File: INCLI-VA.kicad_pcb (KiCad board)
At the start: 2 copper layers, 100 x 100 mm, 168 parts, among them J1 MSTBV 2,5/5-GF-5,08, J2 MSTBV 2,5/2-GF-5,08, J401 USB4105-GF-A, J402 UART0, Q101 STD18NF25, Q102 IPD30N10S3L-34, Q701 DMN10H220LQ, Q751 DMN10H220LQ, SW401 RESET, SW402 BOOT, U101 LM74930QRGERQ1, U201 LMR38010SQDDARQ1, U301 TPS62A02QDRLRQ1, U302 LP5907QMFX-3.3Q1, U401 ESP32-S3-WROOM-1-N8R2, U402 USBLC6-2SC6, U501 SCL3300-D01, U502 ASM330LHHTR, U503 AS5147U-HTSM, U601 ADM3055E, U701 74AHCT1G126, U751 74AHCT1G126, U801 TPS3828-33Q1

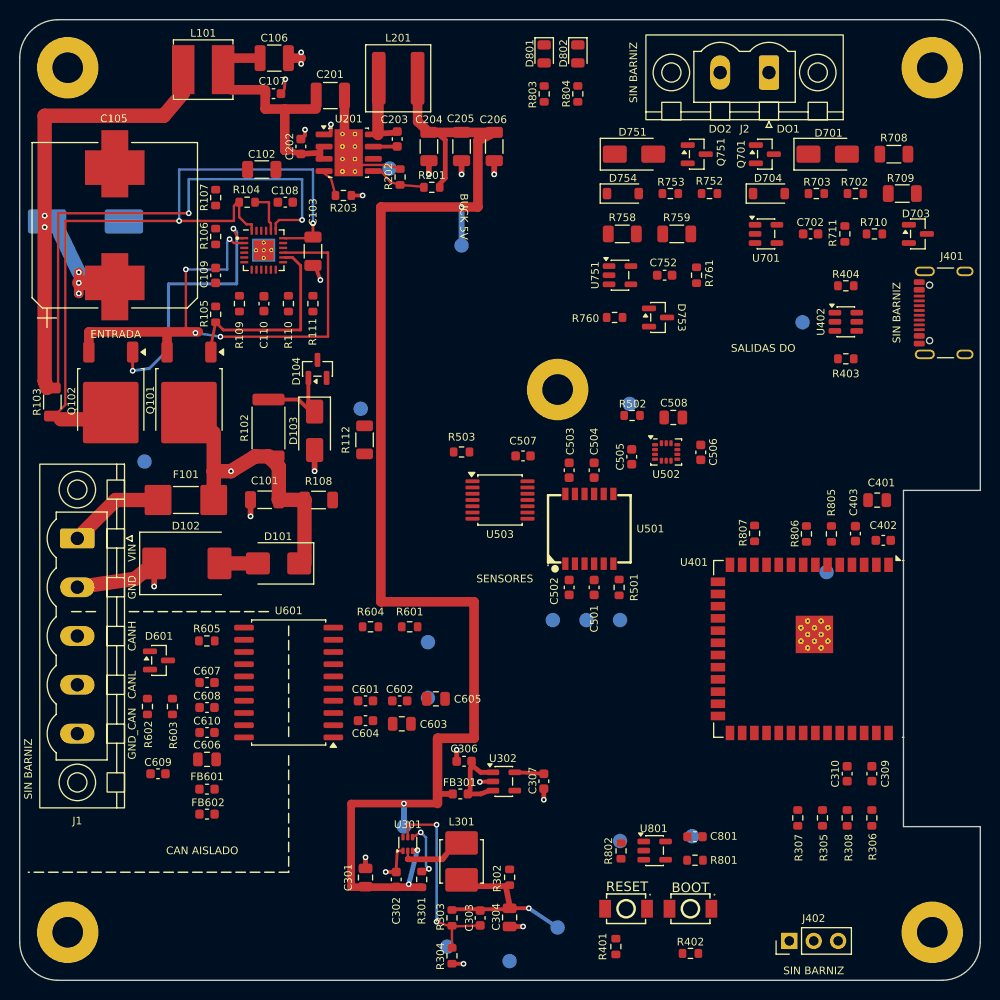
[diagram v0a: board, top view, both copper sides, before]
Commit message: [Claude Code] ruteo etapa 1 (cierre): net class PROT, lazo de U201 en F.Cu, U301 girado, gates paralelos y traspaso a Codex
- Net class PROT (VA, C_ID, VOUT, +VPROT) a 0.6 mm; HV solo VIN_VEH/VBAT_F (1.25 mm).
- ZONA_BUCK_U201 a 0.25 mm: retorno de C202 directo al pin 1 y EP (lazo 6.1 -> 3.9 mm2);
  C201 -> VIN 11.3 -> 8.6 mm.
- U301 girado 180 grados y C302 junto a VIN: SW al norte en F.Cu, EN/FB/PG al sur sin cruzarlo.
- TP101 a (127.6, 61.5) conectado a +VPROT.
- HGATE paralela a OUT/VA; DGATE por B.Cu bajo el retorno de A/VA.
- C104 sigue en B.Cu; caja con separadores >= 12 mm y adhesivo en C104.
- docs/RUTEO_TRASPASO.md: estado, reglas, restricciones, plan de etapas 2-6 y trampas.
- DRC 0 errores, paridad 0, 288 sin rutear.

Co-Authored-By: Claude Opus 5.5 <noreply@anthropic.com>
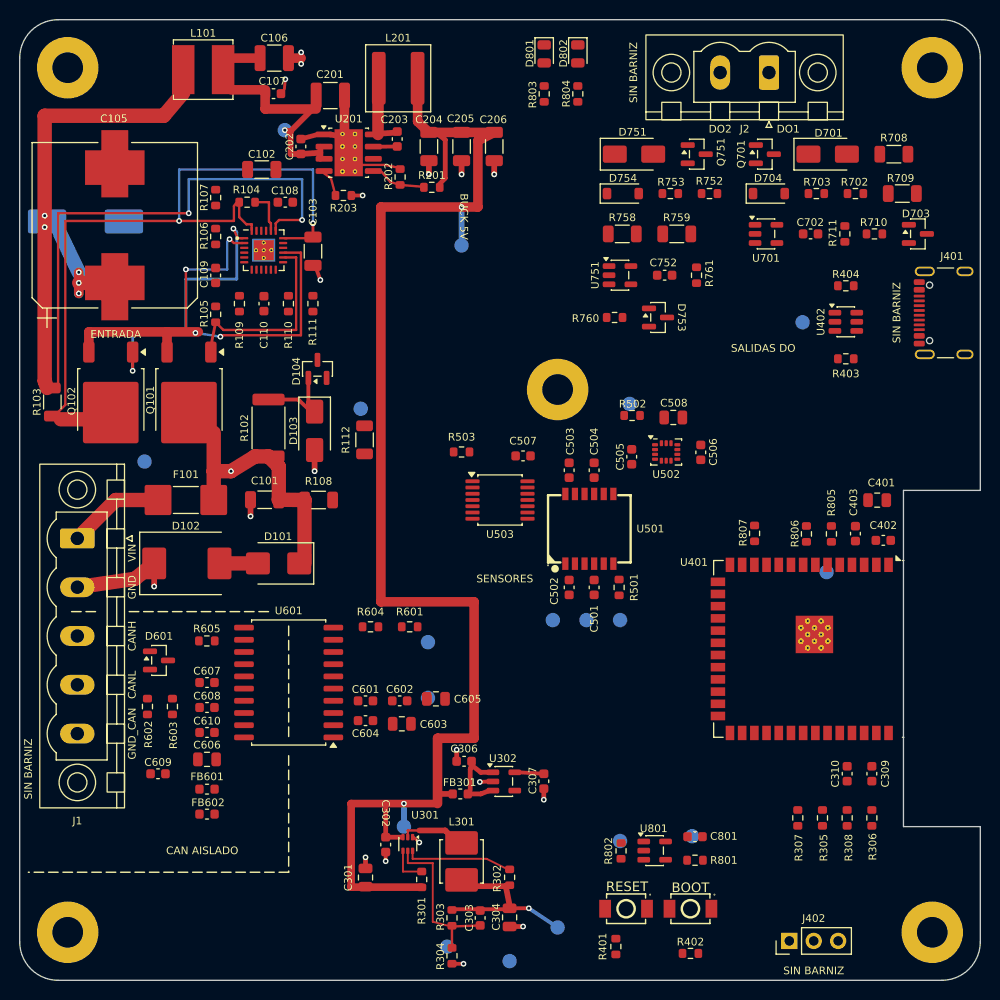
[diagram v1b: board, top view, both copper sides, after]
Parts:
- moved TP101 11.6 mm to (127.6, 61.5)
- moved C302 3.79 mm to (138.1, 135.9), turned to -90 degrees
- turned U301 to -90 degrees
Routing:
- net /30_regulation/PG_3V3D: track 0.00 -> 11.0 mm
- net /10_power_input/VA: track 58.2 -> 52.5 mm
- net Net-(U301-FB): track 20.7 -> 16.9 mm, vias 2 -> 0
- net Net-(U301-EN): track 5.80 -> 3.66 mm, vias 2 -> 0
- net /10_power_input/DGATE: track 27.9 -> 29.3 mm
- net +VPROT: track 22.6 -> 23.8 mm, vias 0 -> 1
- net +5V_VEH: track 147.4 -> 148.1 mm, vias 4 -> 2
- net GND_VEH: track 40.3 -> 40.4 mm, vias 20 -> 19
